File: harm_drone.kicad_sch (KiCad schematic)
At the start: 12 parts, among them IC1 Microcontroller, J1 SYS_DEBUG

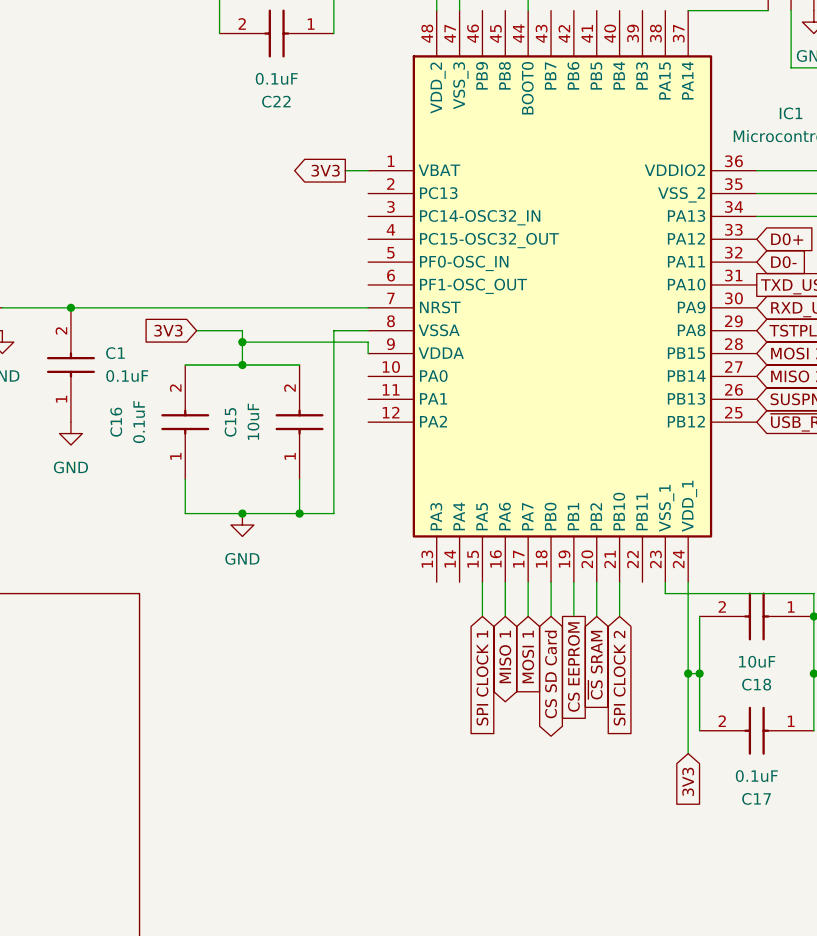
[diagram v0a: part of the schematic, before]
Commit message: add PWM LED
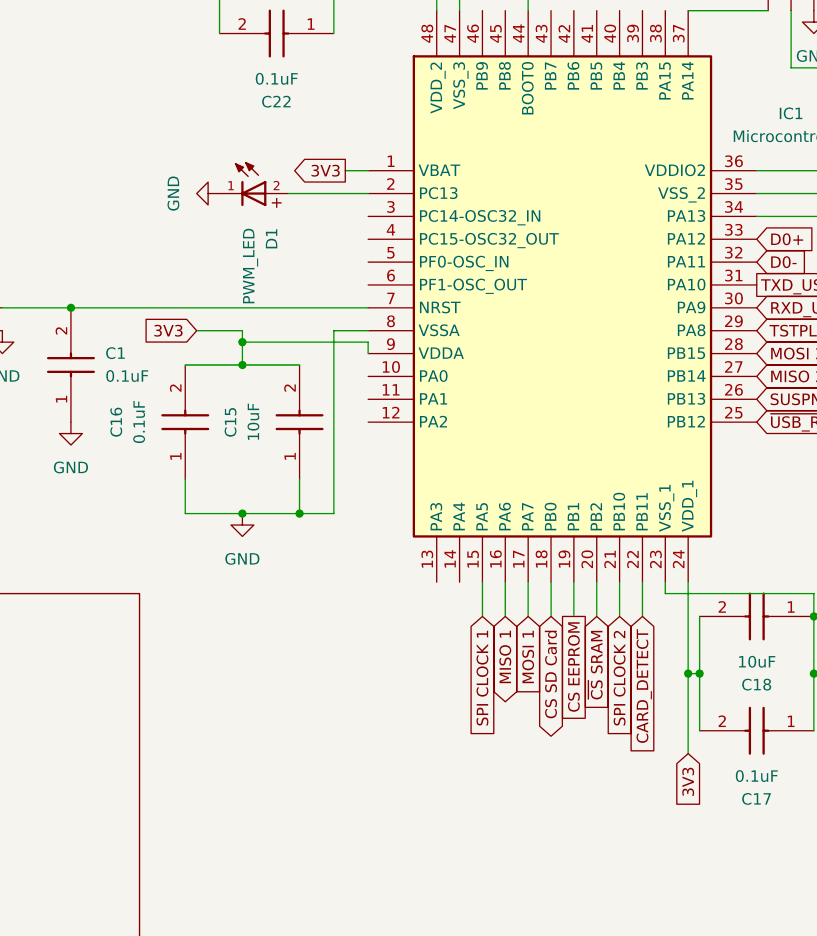
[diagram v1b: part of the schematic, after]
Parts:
- added D1: PWM_LED, group127:PWM_LED, symbol group127:PWM_LED
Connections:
- net GND: now also D1.1
- net at IC1.2 (PC13): now also D1.2
- net CARD_DETECT: now reaches IC1.22 (PB11)
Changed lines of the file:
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@@
+	(wire
+		(pts
+			(xy 148.59 147.32) (xy 148.59 143.51)
+		)
+		(stroke
+			(width 0)
+			(type default)
+		)
+	)
 	(wire
 		(pts
@@
 		(pts
 			(xy 97.79 119.38) (xy 104.14 119.38)
+		)
+		(stroke
+			(width 0)
+			(type default)
+		)
+	)
+	(wire
+		(pts
+			(xy 109.22 100.33) (xy 118.11 100.33)
 		)
 		(stroke
@@
 		(property "Intersheetrefs" "${INTERSHEET_REFS}"
 			(at 161.29 125.73 0)
+			(effects
+				(font
+					(size 1.27 1.27)
+				)
+				(hide yes)
+			)
+		)
+	)
+	(global_label "CARD_DETECT"
+		(shape input)
+		(at 148.59 147.32 270)
+		(effects
+			(font
+				(size 1.27 1.27)
+			)
+			(justify right)
+		)
+		(property "Intersheetrefs" "${INTERSHEET_REFS}"
+			(at 148.59 147.32 0)
 			(effects
 				(font
@@
 	)
 	(symbol
+		(lib_id "power:GND")
+		(at 101.6 100.33 270)
+		(unit 1)
+		(exclude_from_sim no)
+		(in_bom yes)
+		(on_board yes)
+		(dnp no)
+		(fields_autoplaced yes)
+		(property "Reference" "#PWR021"
+			(at 95.25 100.33 0)
+			(effects
+				(font
+					(size 1.27 1.27)
+				)
+				(hide yes)
+			)
+		)
+		(property "Value" "GND"
+			(at 96.52 100.33 0)
+			(effects
+				(font
+					(size 1.27 1.27)
+				)
+			)
+		)
+		(property "Footprint" ""
+			(at 101.6 100.33 0)
+			(effects
+				(font
+					(size 1.27 1.27)
+				)
+				(hide yes)
+			)
+		)
+		(property "Datasheet" ""
+			(at 101.6 100.33 0)
+			(effects
+				(font
+					(size 1.27 1.27)
+				)
+				(hide yes)
+			)
+		)
+		(property "Description" "Power symbol creates a global label with name \"GND\" , ground"
+			(at 101.6 100.33 0)
+			(effects
+				(font
+					(size 1.27 1.27)
+				)
+				(hide yes)
+			)
+		)
+		(pin "1"
+		)
+		(instances
+			(project "harm_drone"
+				(path "/5ce3566e-4e0f-420e-9b0d-3952cd3c63fd"
+					(reference "#PWR021")
+					(unit 1)
+				)
+			)
+		)
+	)
+	(symbol
 		(lib_id "group127:Microcontroller")
 		(at 118.11 97.79 0)
@@
 					(unit 1)
 				)
+			)
+		)
+	)
+	(symbol
+		(lib_id "group127:PWM_LED")
+		(at 104.14 100.33 0)
+		(unit 1)
+		(exclude_from_sim no)
+		(in_bom yes)
+		(on_board yes)
+		(dnp no)
+		(fields_autoplaced yes)
+		(property "Reference" "D1"
+			(at 107.4284 104.14 90)
+			(effects
+				(font
+					(size 1.27 1.27)
+				)
+				(justify right)
+			)
+		)
+		(property "Value" "PWM_LED"
+			(at 104.8884 104.14 90)
+			(effects
+				(font
+					(size 1.27 1.27)
+				)
+				(justify right)
+			)
+		)
+		(property "Footprint" "group127:PWM_LED"
+			(at 104.14 100.33 0)
+			(effects
+				(font
+					(size 1.27 1.27)
+				)
+				(justify bottom)
+				(hide yes)
+			)
+		)
+		(property "Datasheet" ""
+			(at 104.14 100.33 0)
+			(effects
+				(font
+					(size 1.27 1.27)
+				)
+				(hide yes)
+			)
+		)
+		(property "Description" ""
+			(at 104.14 100.33 0)
+			(effects
+				(font
+					(size 1.27 1.27)
+				)
+				(hide yes)
+			)
+		)
+		(pin "1"
+		)
+		(pin "2"
+		)
+		(instances
+			(project ""
+				(path "/5ce3566e-4e0f-420e-9b0d-3952cd3c63fd"
+					(reference "D1")
+					(unit 1)
+				)

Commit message: before model updates
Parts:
- added H1, H2: MountingHole, MountingHole:MountingHole_3.2mm_M3, symbol Mechanical:MountingHole
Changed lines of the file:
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@@
+	)
+	(symbol
+		(lib_id "Mechanical:MountingHole")
+		(at 240.03 83.82 0)
+		(unit 1)
+		(exclude_from_sim yes)
+		(in_bom no)
+		(on_board yes)
+		(dnp no)
+		(fields_autoplaced yes)
+		(property "Reference" "H1"
+			(at 242.57 82.5499 0)
+			(effects
+				(font
+					(size 1.27 1.27)
+				)
+				(justify left)
+			)
+		)
+		(property "Value" "MountingHole"
+			(at 242.57 85.0899 0)
+			(effects
+				(font
+					(size 1.27 1.27)
+				)
+				(justify left)
+			)
+		)
+		(property "Footprint" "MountingHole:MountingHole_3.2mm_M3"
+			(at 240.03 83.82 0)
+			(effects
+				(font
+					(size 1.27 1.27)
+				)
+				(hide yes)
+			)
+		)
+		(property "Datasheet" "~"
+			(at 240.03 83.82 0)
+			(effects
+				(font
+					(size 1.27 1.27)
+				)
+				(hide yes)
+			)
+		)
+		(property "Description" "Mounting Hole without connection"
+			(at 240.03 83.82 0)
+			(effects
+				(font
+					(size 1.27 1.27)
+				)
+				(hide yes)
+			)
+		)
+		(instances
+			(project ""
+				(path "/5ce3566e-4e0f-420e-9b0d-3952cd3c63fd"
+					(reference "H1")
+					(unit 1)
+				)
+			)
+		)
 	)
 	(symbol
@@
 					(unit 1)
 				)
+			)
+		)
+	)
+	(symbol
+		(lib_id "Mechanical:MountingHole")
+		(at 240.03 91.44 0)
+		(unit 1)
+		(exclude_from_sim yes)
+		(in_bom no)
+		(on_board yes)
+		(dnp no)
+		(fields_autoplaced yes)
+		(property "Reference" "H2"
+			(at 242.57 90.1699 0)
+			(effects
+				(font
+					(size 1.27 1.27)
+				)
+				(justify left)
+			)
+		)
+		(property "Value" "MountingHole"
+			(at 242.57 92.7099 0)
+			(effects
+				(font
+					(size 1.27 1.27)
+				)
+				(justify left)
+			)
+		)
+		(property "Footprint" "MountingHole:MountingHole_3.2mm_M3"
+			(at 240.03 91.44 0)
+			(effects
+				(font
+					(size 1.27 1.27)
+				)
+				(hide yes)
+			)
+		)
+		(property "Datasheet" "~"
+			(at 240.03 91.44 0)
+			(effects
+				(font
+					(size 1.27 1.27)
+				)
+				(hide yes)
+			)
+		)
+		(property "Description" "Mounting Hole without connection"
+			(at 240.03 91.44 0)
+			(effects
+				(font
+					(size 1.27 1.27)
+				)
+				(hide yes)
+			)
+		)
+		(instances
+			(project "harm_drone"
+				(path "/5ce3566e-4e0f-420e-9b0d-3952cd3c63fd"
+					(reference "H2")
+					(unit 1)
+				)

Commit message: schematic fixes are done
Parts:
- removed C19: 10uF, Capacitor_SMD:C_0805_2012Metric, symbol group127:0805Capacitor
- removed C20: 0.1uF, Capacitor_SMD:C_0805_2012Metric, symbol group127:0805Capacitor
- added C28, C29, C30, C32: 0.1uF, Capacitor_SMD:C_0805_2012Metric, symbol group127:0805Capacitor
- added C31, C33: 4.7uF, Capacitor_SMD:C_0805_2012Metric, symbol group127:0805Capacitor
- C15: value 10uF -> 10nF
- C18, C21: value 10uF -> 0.1uF
- C22: value 0.1uF -> 4.7uF
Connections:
- net 3V3: now also C15.1, C21.2, C22.2, C28.2, C29.2, C30.2, C31.2, C32.2, C33.2; no longer C15.2, C21.1, C22.1, IC1.1 (VBAT)
- net GND: now also C15.2, C21.1, C22.1, C28.1, C29.1, C30.1, C31.1, C32.1, C33.1; no longer C15.1, C21.2, C22.2

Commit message: final changes
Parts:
- renumbered C30 to C10, C31 to C11, C32 to C12, C33 to C13, C17 to C2, C18 to C3, C15 to C4, C21 to C5, C16 to C6, C22 to C7, C28 to C8, C29 to C9
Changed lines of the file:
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@@
 		(dnp no)
 		(fields_autoplaced yes)
-		(property "Reference" "C32"
+		(property "Reference" "C12"
 			(at 187.96 96.5199 90)
 			(effects
@@
 			(project "harm_drone"
 				(path "/5ce3566e-4e0f-420e-9b0d-3952cd3c63fd"
-					(reference "C32")
+					(reference "C12")
 					(unit 1)
 				)
@@
 		(dnp no)
 		(fields_autoplaced yes)
-		(property "Reference" "C31"
+		(property "Reference" "C11"
 			(at 177.8 153.6699 90)
 			(effects
@@
 			(project "harm_drone"
 				(path "/5ce3566e-4e0f-420e-9b0d-3952cd3c63fd"
-					(reference "C31")
+					(reference "C11")
 					(unit 1)
 				)
@@
 		(dnp no)
 		(fields_autoplaced yes)
-		(property "Reference" "C33"
+		(property "Reference" "C13"
 			(at 195.58 96.5199 90)
 			(effects
@@
 			(project "harm_drone"
 				(path "/5ce3566e-4e0f-420e-9b0d-3952cd3c63fd"
-					(reference "C33")
+					(reference "C13")
 					(unit 1)
 				)
@@
 		(dnp no)
 		(fields_autoplaced yes)
-		(property "Reference" "C29"
+		(property "Reference" "C9"
 			(at 165.1 153.6699 90)
 			(effects
@@
 			(project "harm_drone"
 				(path "/5ce3566e-4e0f-420e-9b0d-3952cd3c63fd"
-					(reference "C29")
+					(reference "C9")
 					(unit 1)
 				)
@@
 		(dnp no)
 		(fields_autoplaced yes)
-		(property "Reference" "#PWR05"
+		(property "Reference" "#PWR06"
 			(at 138.43 78.74 0)
 			(effects
@@
 			(project "harm_drone"
 				(path "/5ce3566e-4e0f-420e-9b0d-3952cd3c63fd"
-					(reference "#PWR05")
+					(reference "#PWR06")
 					(unit 1)
 				)
@@
 		(dnp no)
 		(fields_autoplaced yes)
-		(property "Reference" "#PWR06"
+		(property "Reference" "#PWR05"
 			(at 104.14 140.97 0)
 			(effects
@@
 			(project "harm_drone"
 				(path "/5ce3566e-4e0f-420e-9b0d-3952cd3c63fd"
-					(reference "#PWR06")
+					(reference "#PWR05")
 					(unit 1)
 				)
@@
 		(dnp no)
 		(fields_autoplaced yes)
-		(property "Reference" "#PWR04"
+		(property "Reference" "#PWR09"
 			(at 187.96 110.49 0)
 			(effects
@@
 			(project "harm_drone"
 				(path "/5ce3566e-4e0f-420e-9b0d-3952cd3c63fd"
-					(reference "#PWR04")
+					(reference "#PWR09")
 					(unit 1)
 				)
@@
 		(dnp no)
 		(fields_autoplaced yes)
-		(property "Reference" "#PWR03"
+		(property "Reference" "#PWR07"
 			(at 165.1 167.64 0)
 			(effects
@@
 			(project "harm_drone"
 				(path "/5ce3566e-4e0f-420e-9b0d-3952cd3c63fd"
-					(reference "#PWR03")
+					(reference "#PWR07")
 					(unit 1)
 				)
@@
 		(dnp no)
 		(fields_autoplaced yes)
-		(property "Reference" "#PWR021"
+		(property "Reference" "#PWR04"
 			(at 95.25 100.33 0)
 			(effects
@@
 			(project "harm_drone"
 				(path "/5ce3566e-4e0f-420e-9b0d-3952cd3c63fd"
-					(reference "#PWR021")
+					(reference "#PWR04")
 					(unit 1)
 				)
@@
 		(dnp no)
 		(fields_autoplaced yes)
-		(property "Reference" "C18"
+		(property "Reference" "C3"
 			(at 99.06 74.9299 90)
 			(effects
@@
 			(project "harm_drone"
 				(path "/5ce3566e-4e0f-420e-9b0d-3952cd3c63fd"
-					(reference "C18")
+					(reference "C3")
 					(unit 1)
 				)
@@
 		(dnp no)
 		(fields_autoplaced yes)
-		(property "Reference" "C30"
+		(property "Reference" "C10"
 			(at 171.45 153.6699 90)
 			(effects
@@
 			(project "harm_drone"
 				(path "/5ce3566e-4e0f-420e-9b0d-3952cd3c63fd"
-					(reference "C30")
+					(reference "C10")
 					(unit 1)
 				)
@@
 		(on_board yes)
 		(dnp no)
-		(property "Reference" "C15"
+		(property "Reference" "C4"
 			(at 92.71 128.27 0)
 			(effects
@@
 			(project "harm_drone"
 				(path "/5ce3566e-4e0f-420e-9b0d-3952cd3c63fd"
-					(reference "C15")
+					(reference "C4")
 					(unit 1)
 				)
@@
 		(dnp no)
 		(fields_autoplaced yes)
-		(property "Reference" "C16"
+		(property "Reference" "C6"
 			(at 110.49 126.9999 90)
 			(effects
@@
 			(project "harm_drone"
 				(path "/5ce3566e-4e0f-420e-9b0d-3952cd3c63fd"
-					(reference "C16")
+					(reference "C6")
 					(unit 1)
 				)
@@
 		(dnp no)
 		(fields_autoplaced yes)
-		(property "Reference" "C22"
+		(property "Reference" "C7"
 			(at 111.76 74.9299 90)
 			(effects
@@
 			(project "harm_drone"
 				(path "/5ce3566e-4e0f-420e-9b0d-3952cd3c63fd"
-					(reference "C22")
+					(reference "C7")
 					(unit 1)
 				)
@@
 		(on_board yes)
 		(dnp no)
-		(property "Reference" "C28"
+		(property "Reference" "C8"
 			(at 158.75 153.6699 90)
 			(effects
@@
 			(project "harm_drone"
 				(path "/5ce3566e-4e0f-420e-9b0d-3952cd3c63fd"
-					(reference "C28")
+					(reference "C8")
 					(unit 1)
 				)
@@
 		(on_board yes)
 		(dnp no)
-		(property "Reference" "C17"
+		(property "Reference" "C2"
 			(at 92.71 74.9299 90)
 			(effects
@@
 			(project "harm_drone"
 				(path "/5ce3566e-4e0f-420e-9b0d-3952cd3c63fd"
-					(reference "C17")
+					(reference "C2")
 					(unit 1)
 				)
@@
 		(dnp no)
 		(fields_autoplaced yes)
-		(property "Reference" "#PWR08"
+		(property "Reference" "#PWR03"
 			(at 99.06 88.9 0)
 			(effects
@@
 			(project "harm_drone"
 				(path "/5ce3566e-4e0f-420e-9b0d-3952cd3c63fd"
-					(reference "#PWR08")
+					(reference "#PWR03")
 					(unit 1)
 				)
@@
 		(dnp no)
 		(fields_autoplaced yes)
-		(property "Reference" "C21"
+		(property "Reference" "C5"
 			(at 105.41 74.9299 90)
 			(effects
@@
 			(project "harm_drone"
 				(path "/5ce3566e-4e0f-420e-9b0d-3952cd3c63fd"
-					(reference "C21")
+					(reference "C5")
 					(unit 1)
 				)
@@
 		(dnp no)
 		(fields_autoplaced yes)
-		(property "Reference" "#PWR07"
+		(property "Reference" "#PWR08"
 			(at 167.64 86.36 0)
 			(effects
@@
 			(project "harm_drone"
 				(path "/5ce3566e-4e0f-420e-9b0d-3952cd3c63fd"
-					(reference "#PWR07")
+					(reference "#PWR08")
 					(unit 1)
 				)

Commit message: USB stack changes
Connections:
- net D0+: no longer names the net of IC1.33 (PA12)
- net D0-: no longer names the net of IC1.32 (PA11)
- net TSTPLL/48MCLK: no longer names the net of IC1.29 (PA8)
- no-connect marks 0 -> 3
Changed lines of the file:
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@@
 		(color 0 0 0 0)
+	)
+	(no_connect
+		(at 161.29 115.57)
+	)
+	(no_connect
+		(at 161.29 105.41)
+	)
+	(no_connect
+		(at 161.29 107.95)
 	)
 	(wire
@@
 		)
 	)
-	(global_label "D0-"
-		(shape input)
-		(at 161.29 107.95 0)
-		(effects
-			(font
-				(size 1.27 1.27)
-			)
-			(justify left)
-		)
-		(property "Intersheetrefs" "${INTERSHEET_REFS}"
-			(at 161.29 107.95 0)
-			(effects
-				(font
-					(size 1.27 1.27)
-				)
-				(hide yes)
-			)
-		)
-	)
 	(global_label "3V3"
 		(shape output)
@@
 		)
 	)
-	(global_label "D0+"
-		(shape input)
-		(at 161.29 105.41 0)
-		(effects
-			(font
-				(size 1.27 1.27)
-			)
-			(justify left)
-		)
-		(property "Intersheetrefs" "${INTERSHEET_REFS}"
-			(at 161.29 105.41 0)
-			(effects
-				(font
-					(size 1.27 1.27)
-				)
-				(hide yes)
-			)
-		)
-	)
 	(global_label "SPI CLOCK 1"
 		(shape input)
@@
 				(hide yes)
 			)
-		)
-	)
-	(global_label "TSTPLL/48MCLK"
-		(shape input)
-		(at 161.29 115.57 0)
-		(effects
-			(font
-				(size 1.27 1.27)
-			)
-			(justify left)
-		)
-		(property "Intersheetrefs" "${INTERSHEET_REFS}"
-			(at 161.29 115.57 90)
-			(effects
-				(font
-					(size 1.27 1.27)
-				)
-				(justify left)
-				(hide yes)
-			)
